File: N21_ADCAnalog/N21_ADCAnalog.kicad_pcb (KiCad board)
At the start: 2 copper layers, 96.5 x 63.3 mm, 60 parts

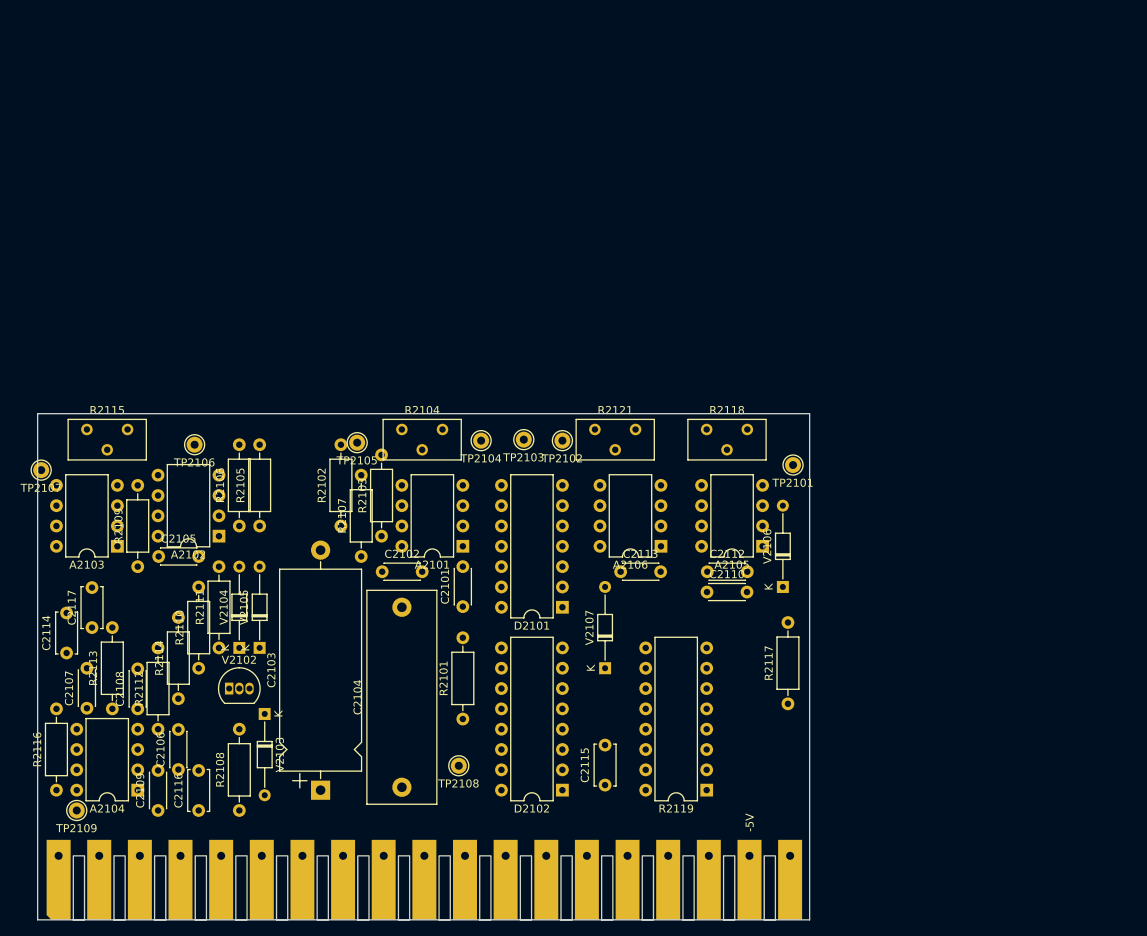
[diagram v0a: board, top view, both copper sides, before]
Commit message: Added N22/N23
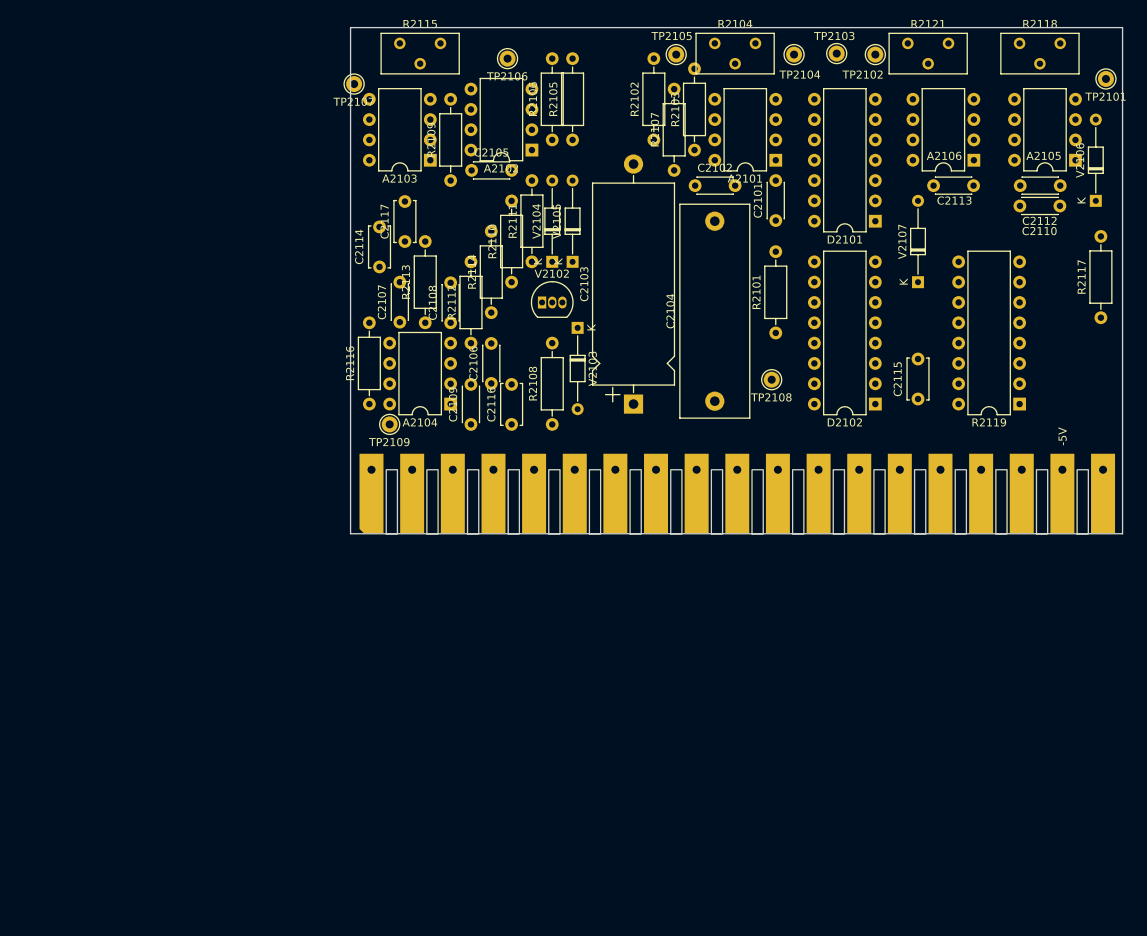
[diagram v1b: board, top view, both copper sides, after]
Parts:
- moved TP2105 62.8 mm to (147.3, 69.3)
- moved C2102 62.1 mm to (149.7, 85.7)
- moved C2105 62.1 mm to (121.7, 83.8)
- moved C2109 62.1 mm to (121.7, 115.6)
- moved C2113 62.1 mm to (179.5, 85.7)
- moved C2116 62.1 mm to (126.7, 115.6)
- moved R2107 62.1 mm to (147.1, 83.8)
- moved R2108 62.1 mm to (131.8, 115.6)
- moved R2114 62.1 mm to (124.2, 101.6)
- moved TP2109 62.1 mm to (111.5, 115.6)
- moved A2106 62.1 mm to (184.5, 82.5)
- moved C2110 62.1 mm to (190.3, 88.3)
- moved C2112 62.1 mm to (190.3, 85.7)
- moved R2102 62.1 mm to (144.5, 80.0)
- moved R2105 62.1 mm to (134.4, 80.0)
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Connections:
- net /SAZ renamed /xAZ
- net /SDN+ renamed /xDN+
- net /SDN- renamed /xDN-
- net /SUP renamed /xUP
- C2110 pad 1: +2VRef -> GND3
- C2110 pad 2: GND3 -> +2VRef

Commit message: Updates, add N25
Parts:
- K1: footprint Philips_PM2528:PM2528_RiserCardConnector -> PM2528:PM2528_RiserCardConnector
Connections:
- net +2VRef renamed /+2VRef
- net AZ renamed /AZ
- net DN+ renamed /DN+
- net DN- renamed /DN-
- net INPUT renamed /INPUT
- net UP renamed /UP
- K1 pad 19: COMP -> /COMP
- R2116 pad 2: COMP -> /COMP
- TP2109 pad 1: COMP -> /COMP

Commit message: Small updates, N25 also
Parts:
- R2104, R2115, R2118, R2121: footprint Potentiometer_THT:Potentiometer_Bourns_3296Y_Vertical -> PM2528:Potentiometer horizontal ceramic
- R2119: footprint Package_DIP:DIP-16_W7.62mm -> Package_DIP:DIP-14_W7.62mm_Socket
- moved R2115 2.35 mm to (119.0, 70.0), turned to -90 degrees
- moved R2118 1.69 mm to (194.0, 69.0), turned to -90 degrees
- moved C2117 1.28 mm to (114.5, 93.4)
- moved R2121 1.24 mm to (182.0, 69.0), turned to -90 degrees
- moved R2104 1.08 mm to (157.0, 69.0), turned to -90 degrees
- moved C2114 0.77 mm to (111.0, 96.0)
- moved C2107 0.75 mm to (113.5, 103.0)
- moved C2102 0.72 mm to (149.0, 85.5)
- moved C2115 0.56 mm to (177.0, 112.5)
- moved C2109 0.54 mm to (122.0, 116.0)
- moved C2101 0.49 mm to (159.5, 90.5)
- moved TP2103 0.48 mm to (167.0, 69.5)
- moved C2116 0.27 mm to (127.0, 115.5)
- moved C2108 0.13 mm to (119.0, 102.8)
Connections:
- A2102 pad 1: Net-(A2102-LOGIC_REFERENCE) -> Net-(A2102-BAL)
- A2102 pad 2: Net-(A2102--) -> unconnected-(A2102---Pad2)
- A2102 pad 3: Net-(A2102-+) -> unconnected-(A2102-+-Pad3)
- A2102 pad 6: Net-(A2102-Pad6) -> Net-(A2102-BAL)
- A2104 pad 7: COMP -> /COMP
- C2103 pad 1: Net-(A2102-Pad6) -> Net-(A2102-BAL)
- C2105 pad 1: Net-(A2102-LOGIC_REFERENCE) -> Net-(A2102-BAL)
- R2105 pad 1: Net-(A2102--) -> Net-(V2101-1S)
- R2106 pad 1: Net-(A2102-+) -> Net-(V2101-2S)
- R2109 pad 1: Net-(A2102-Pad6) -> Net-(A2102-BAL)
- TP2106 pad 1: Net-(A2102-Pad6) -> Net-(A2102-BAL)
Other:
- board size 96.5 x 63.3 mm -> 97.5 x 63.3 mm
- board text added: "CAL1"
- board text added: "CAL2"
- board text added: "DBZ"
- board text added: "Zero"

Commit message: Update schematics, move projectlibraries to D:
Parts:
- added C2111: 4n22/63V, Capacitor_THT:C_Axial_L5.1mm_D3.1mm_P15.00mm_Horizontal, F.Cu at (187.0, 88.0)
- added JP1: Jumper_2_Small_Bridged, TestPoint:TestPoint_Bridge_Pitch2.54mm_Drill1.0mm, F.Cu at (192.5, 113.0)
- added JP2: Jumper_2_Small_Bridged, TestPoint:TestPoint_Bridge_Pitch2.54mm_Drill1.0mm, F.Cu at (195.5, 110.5)
- added JP3: Jumper_2_Small_Bridged, TestPoint:TestPoint_Bridge_Pitch2.54mm_Drill1.0mm, F.Cu at (192.5, 108.0)
- added JP4: Jumper_2_Small_Bridged, TestPoint:TestPoint_Bridge_Pitch2.54mm_Drill1.0mm, F.Cu at (195.5, 105.5)
- added R2120: 590, Resistor_THT:R_Axial_DIN0309_L9.0mm_D3.2mm_P12.70mm_Horizontal, F.Cu at (196.5, 103.2)
- added V2101: ~, Package_TO_SOT_THT:TO-78-6, F.Cu at (137.2, 77.8)
- C2101: value 10n -> 10n/100V
- C2102, C2107, C2108, C2109: value 22n -> 22n/63V
- C2103: value 162n -> 162n/100V
- C2104: value 3u3 -> 3u3/100V
- C2105, C2112, C2113: value 33p -> 33p/100V
- C2106: value 220p -> 220p/500V
- C2110: value 4n7 -> 4n7/100V
- C2114, C2117: value 6u8 -> 6u8/25V
- C2115, C2116: value 22u -> 22u/10V
- R2119: value ~ -> OM528
- moved R2119 1.13 mm to (189.1, 113.0)
- moved C2112 0.36 mm to (190.5, 85.4)
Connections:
- A2102 pad 2: unconnected-(A2102---Pad2) -> Net-(A2102--)
- A2102 pad 3: unconnected-(A2102-+-Pad3) -> Net-(A2102-+)
- R2105 pad 1: Net-(V2101-1S) -> Net-(A2102--)
- R2106 pad 1: Net-(V2101-2S) -> Net-(A2102-+)
- R2118 pad 1: Net-(R2118-Pad1) -> Net-(JP4-B)
- R2119 pad 1: Net-(R2119-Pad1) -> Net-(JP1-B)
- R2119 pad 11: Net-(R2118-Pad1) -> Net-(JP4-A)
- R2119 pad 13: Net-(R2119-Pad1) -> Net-(JP3-B)
- R2119 pad 14: Net-(R2119-Pad1) -> Net-(JP1-A)
- R2119 pad 2: Net-(R2119-Pad1) -> Net-(JP2-B)
- R2119 pad 5: Net-(R2118-Pad1) -> Net-(JP4-B)
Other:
- board text added: "A"
- board text added: "B"
- board text added: "C"
- board text added: "CAL+"
- board text added: "CAL-"
- board text added: "D"
- board text removed: "CAL1"
- board text removed: "CAL2"
